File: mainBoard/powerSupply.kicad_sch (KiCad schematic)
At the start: 69 parts, among them J1 1366005, Q8 IRLML6244TRPBF, Q9 IRLML6244TRPBF, SW1 SW_SPST, U1 MCP1727T-3302E/SN, U2 AP62250WU, U3 MCP1727T-3302E/SN, U5 TPS2041B

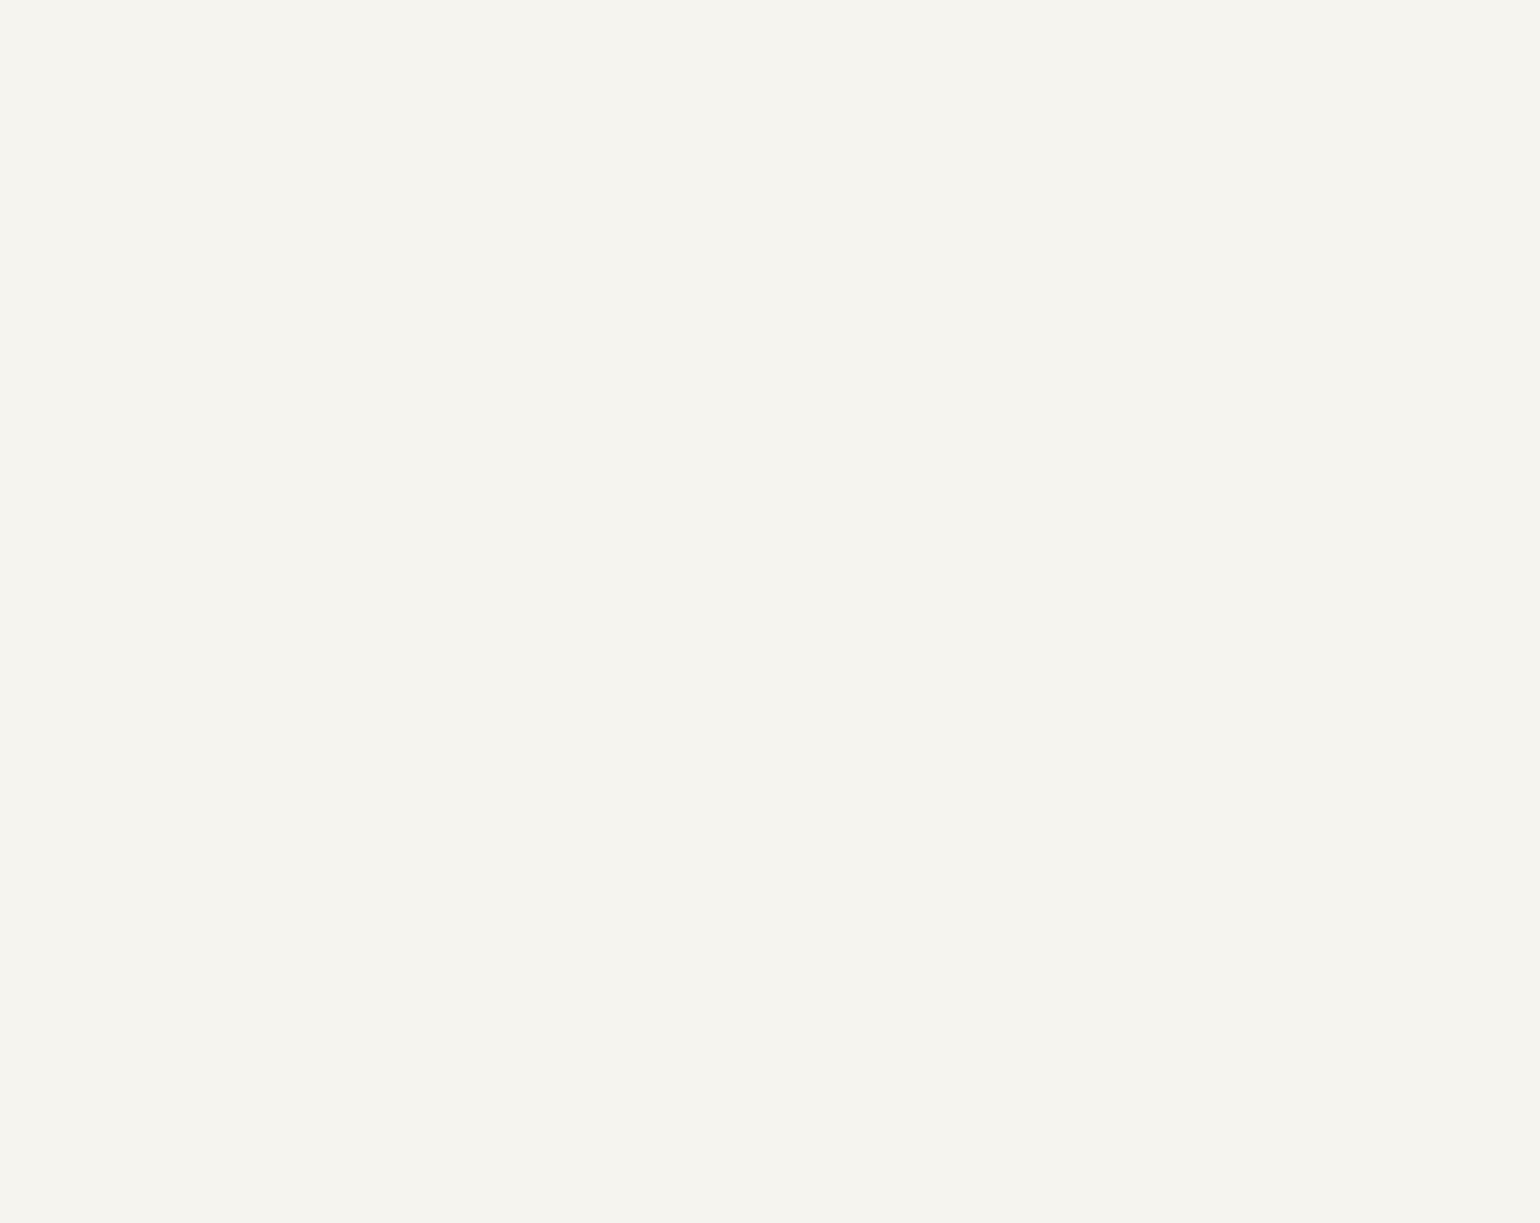
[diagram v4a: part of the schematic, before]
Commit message: updating power supplies to richtek
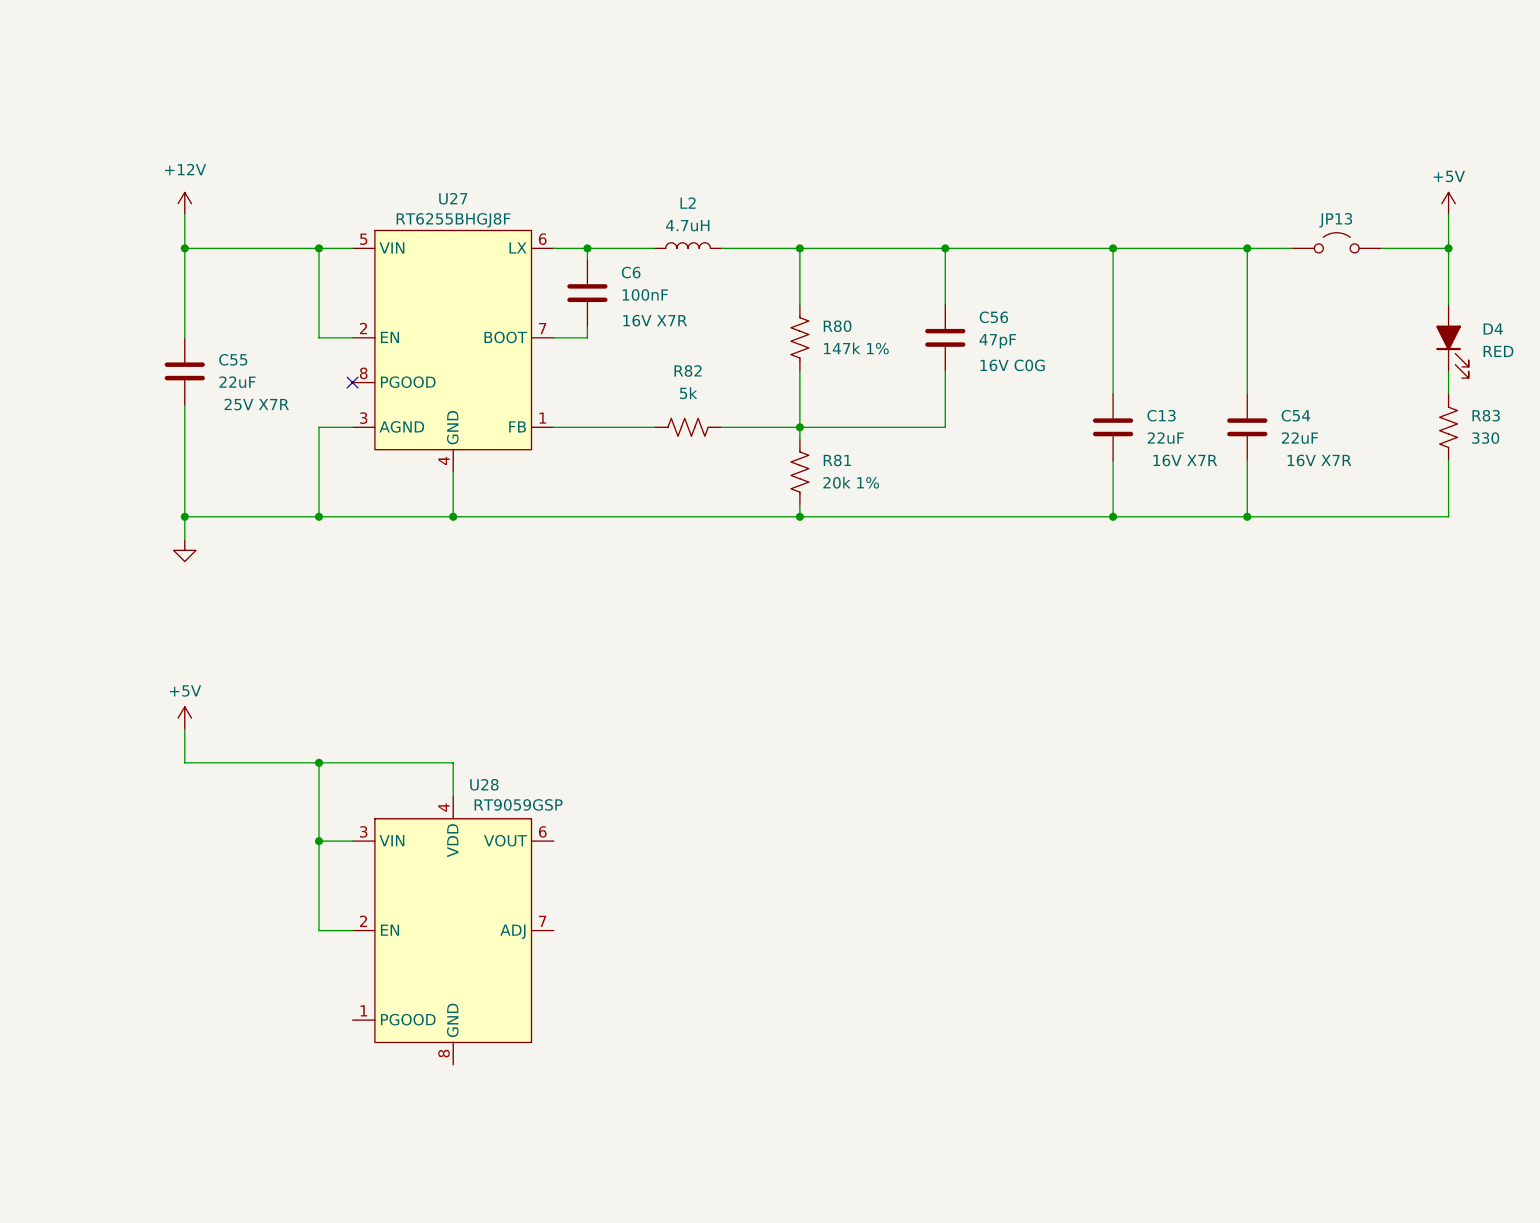
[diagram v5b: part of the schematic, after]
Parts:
- added C13, C54, C55: 22uF, Capacitor_SMD:C_1206_3216Metric_Pad1.33x1.80mm_HandSolder, symbol Device:C
- added C56: 47pF, Capacitor_SMD:C_0603_1608Metric_Pad1.08x0.95mm_HandSolder, symbol Device:C
- added C6: 100nF, Capacitor_SMD:C_0603_1608Metric_Pad1.08x0.95mm_HandSolder, symbol Device:C
- added D4: RED, LED_SMD:LED_0603_1608Metric_Pad1.05x0.95mm_HandSolder, symbol Device:LED_Filled
- added JP13: Jumper_2_Open, Connector_PinHeader_2.54mm:PinHeader_1x02_P2.54mm_Vertical, symbol Jumper:Jumper_2_Open
- added L2: 4.7uH, Inductor_SMD:L_1008_2520Metric_Pad1.43x2.20mm_HandSolder, symbol Device:L
- added R80: 147k 1%, Resistor_SMD:R_0603_1608Metric_Pad0.98x0.95mm_HandSolder, symbol Device:R_US
- added R81: 20k 1%, Resistor_SMD:R_0603_1608Metric_Pad0.98x0.95mm_HandSolder, symbol Device:R_US
- added R82: 5k, Resistor_SMD:R_0603_1608Metric_Pad0.98x0.95mm_HandSolder, symbol Device:R_US
- added R83: 330, Resistor_SMD:R_0603_1608Metric_Pad0.98x0.95mm_HandSolder, symbol Device:R_US
- added U27: RT6255BHGJ8F, Package_TO_SOT_SMD:TSOT-23-8, symbol Richtek:RT6255
- added U28: RT9059GSP, Package_SO:SOP-8-1EP_4.57x4.57mm_P1.27mm_EP4.57x4.45mm, symbol Richtek:RT9059
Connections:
- net +12V: now also C55.1, U27.2 (EN), U27.5 (VIN)
- net +5V: now also D4.2 (A), JP13.2 (B), U28.2 (EN), U28.3 (VIN), U28.4 (VDD)
- net GND: now also C13.2, C54.2, C55.2, R81.2, R83.2, U27.3 (AGND), U27.4 (GND)
- new net: R82.1, U27.1 (FB)
- new net: C56.2, R80.2, R81.1, R82.2
- new net: C6.1, L2.1, U27.6 (LX)
- new net: C13.1, C54.1, C56.1, JP13.1 (A), L2.2, R80.1
- new net: D4.1 (K), R83.1
- new net: C6.2, U27.7 (BOOT)
- no-connect marks 0 -> 1

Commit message: finish changing to richtek power supplies
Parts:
- removed C10, C8: 22uF, Capacitor_SMD:C_1206_3216Metric_Pad1.33x1.80mm_HandSolder, symbol Device:C
- removed C2, C41, C7: 47nF, Capacitor_SMD:C_0603_1608Metric_Pad1.08x0.95mm_HandSolder, symbol Device:C
- removed C3: 100uF, KemetA765:CAPAE830X730N, symbol Device:C_Polarized
- removed C39, C40, C48, C49, C50, C51, C52, C53: 10uF, Capacitor_SMD:C_0805_2012Metric_Pad1.18x1.45mm_HandSolder, symbol Device:C
- removed C42, C5: 100nF, Capacitor_SMD:C_0603_1608Metric_Pad1.08x0.95mm_HandSolder, symbol Device:C
- removed C47: 10uF, Capacitor_SMD:C_1206_3216Metric_Pad1.33x1.80mm_HandSolder, symbol Device:C
- removed D1, D16, D2: RED, LED_SMD:LED_0603_1608Metric_Pad1.05x0.95mm_HandSolder, symbol Device:LED_Filled
- removed JP1, JP2, JP4: Jumper_2_Open, Connector_PinHeader_2.54mm:PinHeader_1x02_P2.54mm_Vertical, symbol Jumper:Jumper_2_Open
- removed L1: 2.2uH, Inductor_SMD:L_1008_2520Metric_Pad1.43x2.20mm_HandSolder, symbol Device:L
- removed Q8, Q9: IRLML6244TRPBF, Package_TO_SOT_SMD:SOT-23, symbol Transistor_FET:IRLML6244
- removed R2, R5, R6: 330, Resistor_SMD:R_0603_1608Metric_Pad0.98x0.95mm_HandSolder, symbol Device:R_US
- removed R3: 52.3k 1%, Resistor_SMD:R_0603_1608Metric_Pad0.98x0.95mm_HandSolder, symbol Device:R_US
- removed R4: 10k 1%, Resistor_SMD:R_0603_1608Metric_Pad0.98x0.95mm_HandSolder, symbol Device:R_US
- removed R71, R72: 10k, Resistor_SMD:R_0603_1608Metric_Pad0.98x0.95mm_HandSolder, symbol Device:R_US
- removed TP3, TP4: TestPoint, TestPoint:TestPoint_Pad_4.0x4.0mm, symbol Connector:TestPoint
- removed U1, U3: MCP1727T-3302E/SN, Package_SO:SOIC-8_3.9x4.9mm_P1.27mm, symbol Regulator_Linear:MCP1727-3302xSN
- removed U2: AP62250WU, Package_TO_SOT_SMD:TSOT-23-6_HandSoldering, symbol Regulator_Switching:AP62250WU
- added C59, C64: 10uF, Capacitor_SMD:C_0805_2012Metric_Pad1.18x1.45mm_HandSolder, symbol Device:C
- added C60, C63: 1uF, Capacitor_SMD:C_0805_2012Metric_Pad1.18x1.45mm_HandSolder, symbol Device:C
- added C61, C62, C65, C66: 22uF, Capacitor_SMD:C_0805_2012Metric_Pad1.18x1.45mm_HandSolder, symbol Device:C
- added D18, D19: RED, LED_SMD:LED_0603_1608Metric_Pad1.05x0.95mm_HandSolder, symbol Device:LED_Filled
- added JP14, JP15: Jumper_2_Open, Connector_PinHeader_2.54mm:PinHeader_1x02_P2.54mm_Vertical, symbol Jumper:Jumper_2_Open
- added R84, R89: 10.5k 1%, Resistor_SMD:R_0603_1608Metric_Pad0.98x0.95mm_HandSolder, symbol Device:R_US
- added R85, R90: 2k 1%, Resistor_SMD:R_0603_1608Metric_Pad0.98x0.95mm_HandSolder, symbol Device:R_US
- added R86, R88: 100k, Resistor_SMD:R_0603_1608Metric_Pad0.98x0.95mm_HandSolder, symbol Device:R_US
- added R87, R91: 330, Resistor_SMD:R_0603_1608Metric_Pad0.98x0.95mm_HandSolder, symbol Device:R_US
- added TP10, TP7: TestPoint, TestPoint:TestPoint_Pad_4.0x4.0mm, symbol Connector:TestPoint
- added U29: RT9059GSP, Package_SO:SOP-8-1EP_4.57x4.57mm_P1.27mm_EP4.57x4.45mm, symbol Richtek:RT9059
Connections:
- net +3.3V: now also D18.2 (A), JP14.2 (B)
- net +3.3VA: now also D19.2 (A), JP15.2 (B), TP7.1
- net +5V: now also C59.1, C60.1, C63.1, C64.1, U29.2 (EN), U29.3 (VIN), U29.4 (VDD)
- net GND: now also U28.8 (GND), C59.2, C60.2, C61.2, C62.2, C63.2, C64.2, C65.2, C66.2, R85.2, R87.2, R90.2, R91.2, TP10.1, U29.8 (GND)
- net at U28.1 (PGOOD): now also R86.1
- net at U28.6 (VOUT): now also C61.1, C62.1, JP14.1 (A), R84.1, R86.2
- net at U28.7 (ADJ): now also R84.2, R85.1
- new net: C65.1, C66.1, JP15.1 (A), R88.2, R89.1, U29.6 (VOUT)
- new net: D19.1 (K), R91.1
- new net: R88.1, U29.1 (PGOOD)
- new net: R89.2, R90.1, U29.7 (ADJ)
- new net: D18.1 (K), R87.1
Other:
- moved on the sheet: C13, C44, C45, C46, C54, C55, C56, C6, D17, D4, H1, H2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

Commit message: change to single 4" touchscreen for UI instead of keypad and buttons
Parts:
- removed H5, H6: MountingHole_Pad, MountingHole:MountingHole_2.7mm, symbol Mechanical:MountingHole
- added FB1: FerriteBead, symbol Device:FerriteBead
- added H1: MountingHole, MountingHole:MountingHole_3.2mm_M3, symbol Mechanical:MountingHole
- added H6, H7, H8: MountingHole_Pad, MountingHole:MountingHole_3.2mm_M3_Pad_Via, symbol Mechanical:MountingHole_Pad
- H2, H3, H4: value MountingHole_Pad -> MountingHole; footprint MountingHole:MountingHole_2.7mm -> MountingHole:MountingHole_3.2mm_M3
- H5: renamed from H1; footprint MountingHole:MountingHole_2.7mm_Pad_Via -> MountingHole:MountingHole_3.2mm_M3_Pad_Via
- renumbered C60 to C1, C54 to C10, C63 to C11, C64 to C12, C9 to C13, C44 to C14, C11 to C15, C12 to C16, C65 to C17, C45 to C18, C66 to C19, C55 to C2, C46 to C20, C59 to C3, C6 to C4, C61 to C5, C56 to C6, C62 to C7, C13 to C8, C43 to C9, D18 to D1, D4 to D2, D19 to D4, D17 to D5, JP14 to JP1, JP13 to JP2, JP10 to JP3, JP12 to JP4, JP3 to JP5, JP15 to JP6, L2 to L1, R86 to R1, R77 to R10, R76 to R11, R88 to R12, R89 to R13, R90 to R14, R7 to R15, R91 to R16, R8 to R17, R82 to R2, R84 to R3, R85 to R4, R80 to R5, R81 to R6, R87 to R7, R73 to R8, R83 to R9, TP7 to TP3, TP10 to TP4, U27 to U1, U28 to U2, U29 to U3, U5 to U4
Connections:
- net +5V: now also FB1.1; no longer C11.1, C12.1, U3.2 (EN), U3.3 (VIN), U3.4 (VDD)
- net GND: now also H6.1, H7.1, H8.1
- new net: C11.1, C12.1, FB1.2, U3.2 (EN), U3.3 (VIN), U3.4 (VDD)
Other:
- moved on the sheet: C11, C12, C17, C19, D4, H5, JP6, R12, R13, R14, R16, TP3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

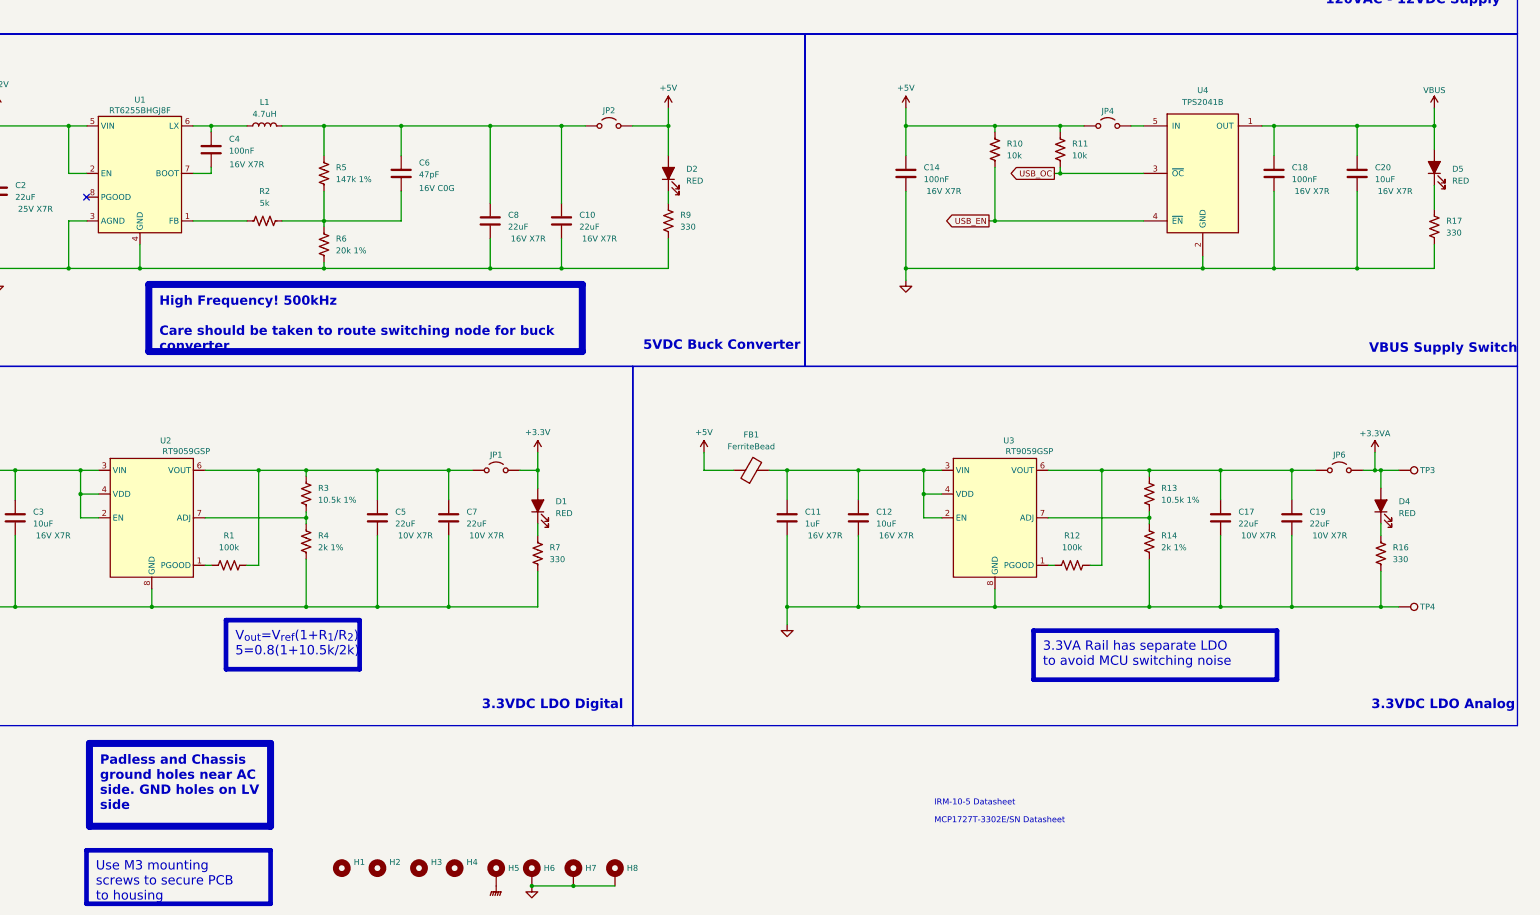
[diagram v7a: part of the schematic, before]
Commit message: change to stm32f413 and add a QSPI SRAM
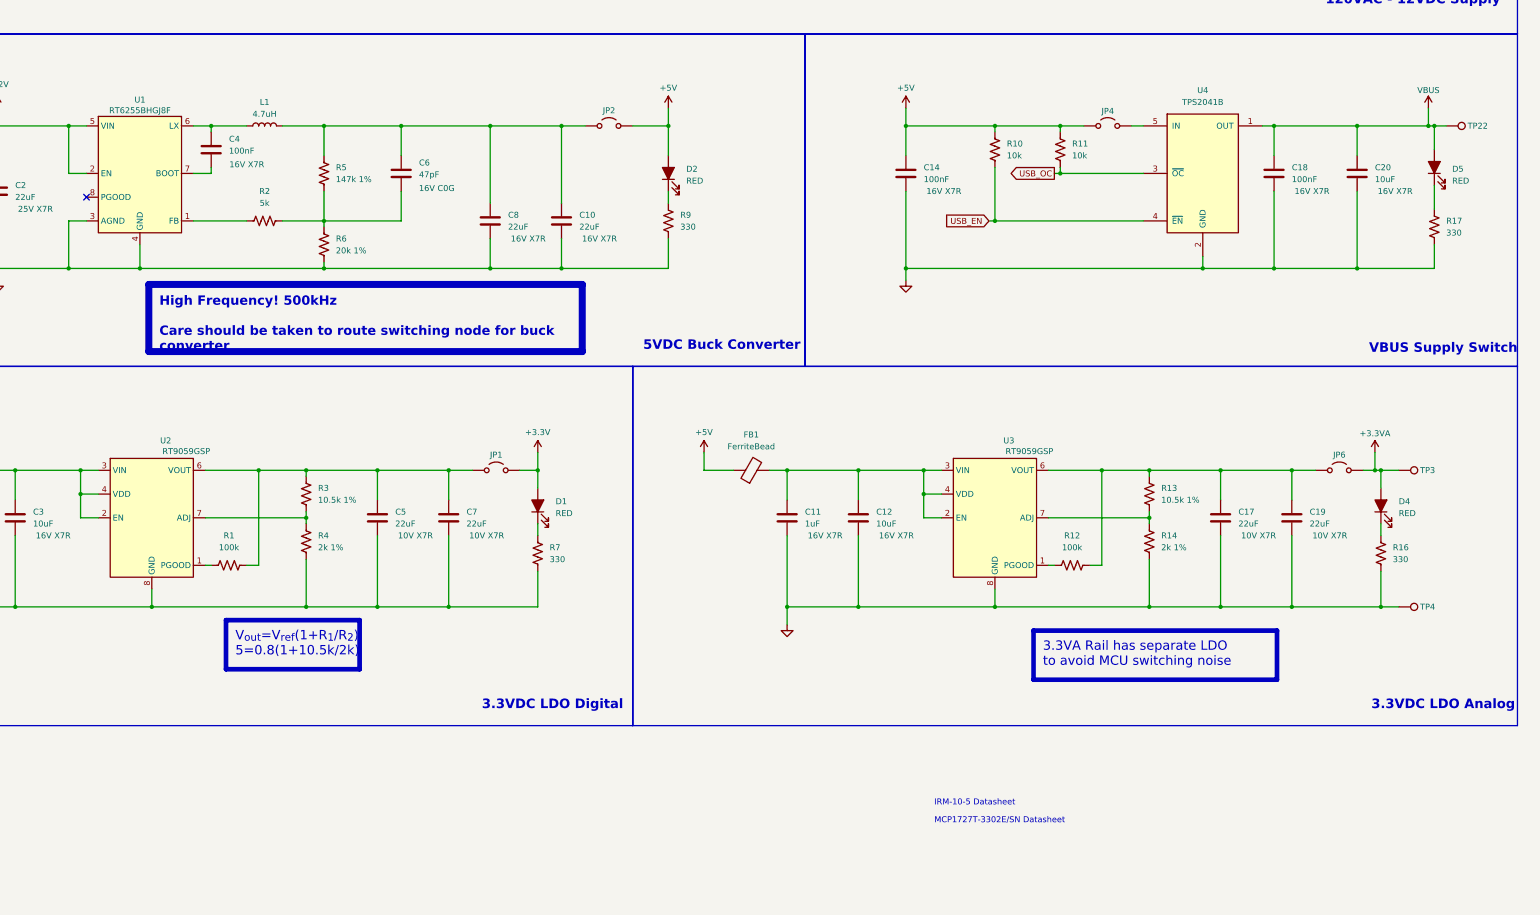
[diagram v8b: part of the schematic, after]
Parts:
- removed H1, H2, H3, H4: MountingHole, MountingHole:MountingHole_3.2mm_M3, symbol Mechanical:MountingHole
- removed H5, H6, H7, H8: MountingHole_Pad, MountingHole:MountingHole_3.2mm_M3_Pad_Via, symbol Mechanical:MountingHole_Pad
- added TP22: TestPoint, TestPoint:TestPoint_Pad_4.0x4.0mm, symbol Connector:TestPoint
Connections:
- net VBUS: now also TP22.1
